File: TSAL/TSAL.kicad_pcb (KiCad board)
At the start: 2 copper layers, 87.6 x 58.1 mm, 59 parts, among them J1 Conn_02x03_Counter_Clockwise, J2 Conn_01x02, J3 Conn_02x01, J4 Conn_02x01, Q1 BSS138, Q2 BSS138, Q3 AO3401A, U1 LM358, U10 74HC74, U2 74HC27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

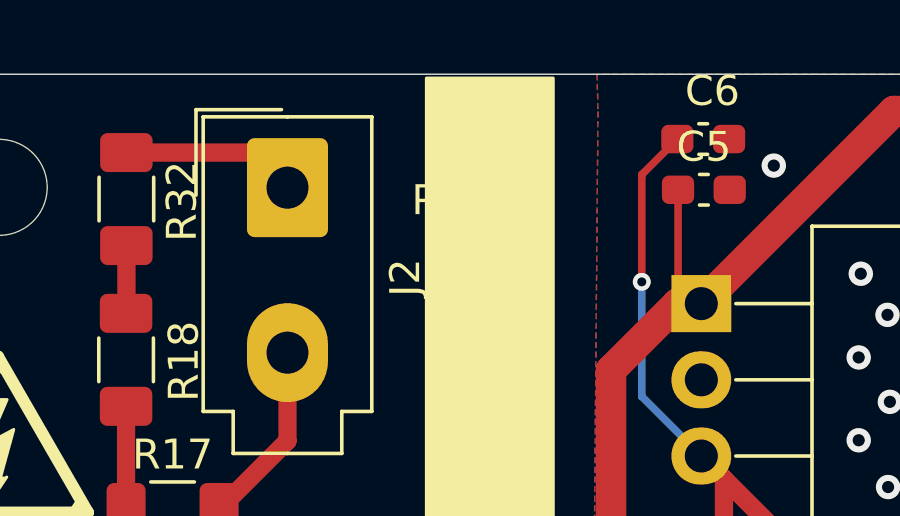
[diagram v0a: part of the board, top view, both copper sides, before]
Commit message: Precharge: cap DC bias correction, PDs on TSAL
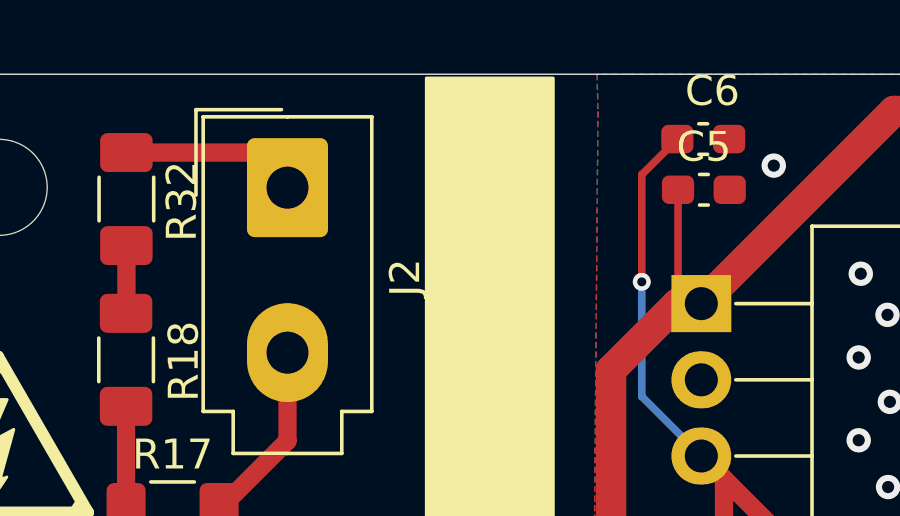
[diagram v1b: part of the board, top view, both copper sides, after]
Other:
- board text removed: "PS1"
